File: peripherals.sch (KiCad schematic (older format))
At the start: 49 parts, among them J1 693022010811, J5 U_FL-R-SMT-1_10_, J6 U_FL-R-SMT-1_10_, J7 DM3AT-SF-PEJM5, U6 NCP163ASN330T1G, U7 EMIF06-MSD02N16

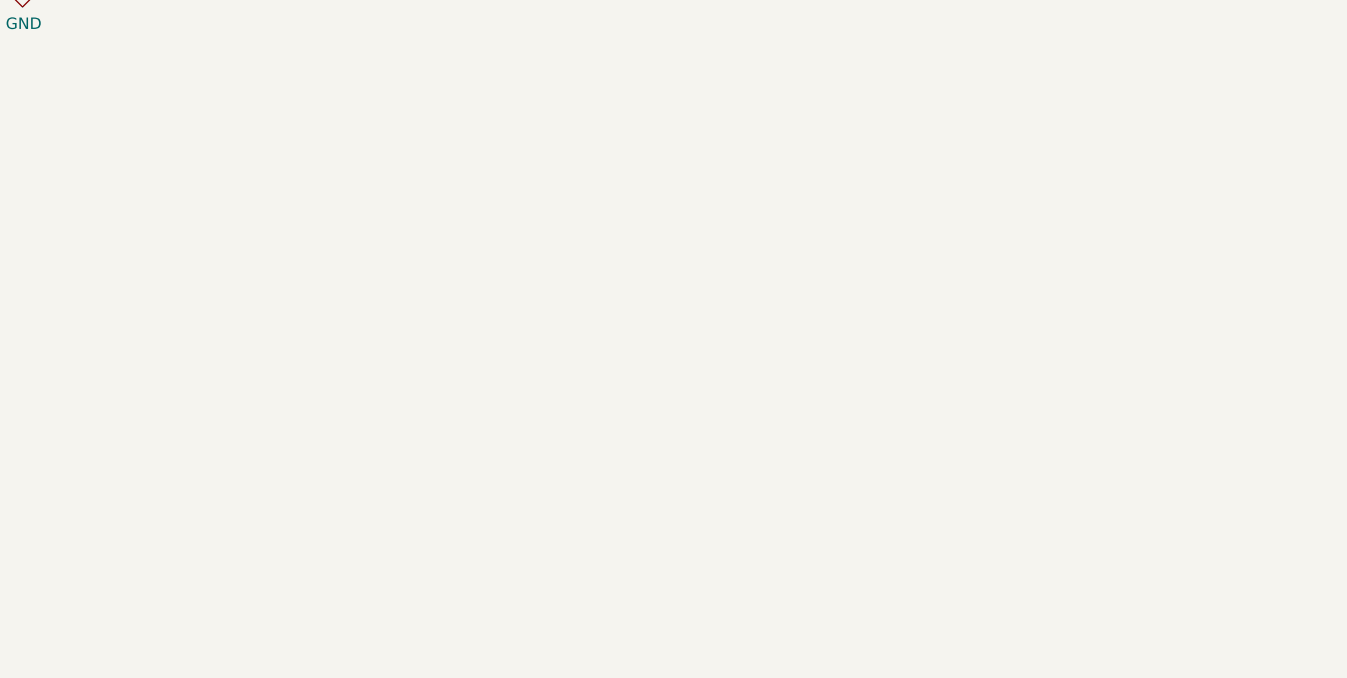
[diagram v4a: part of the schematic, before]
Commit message: Modifications after P. Szczygiel review
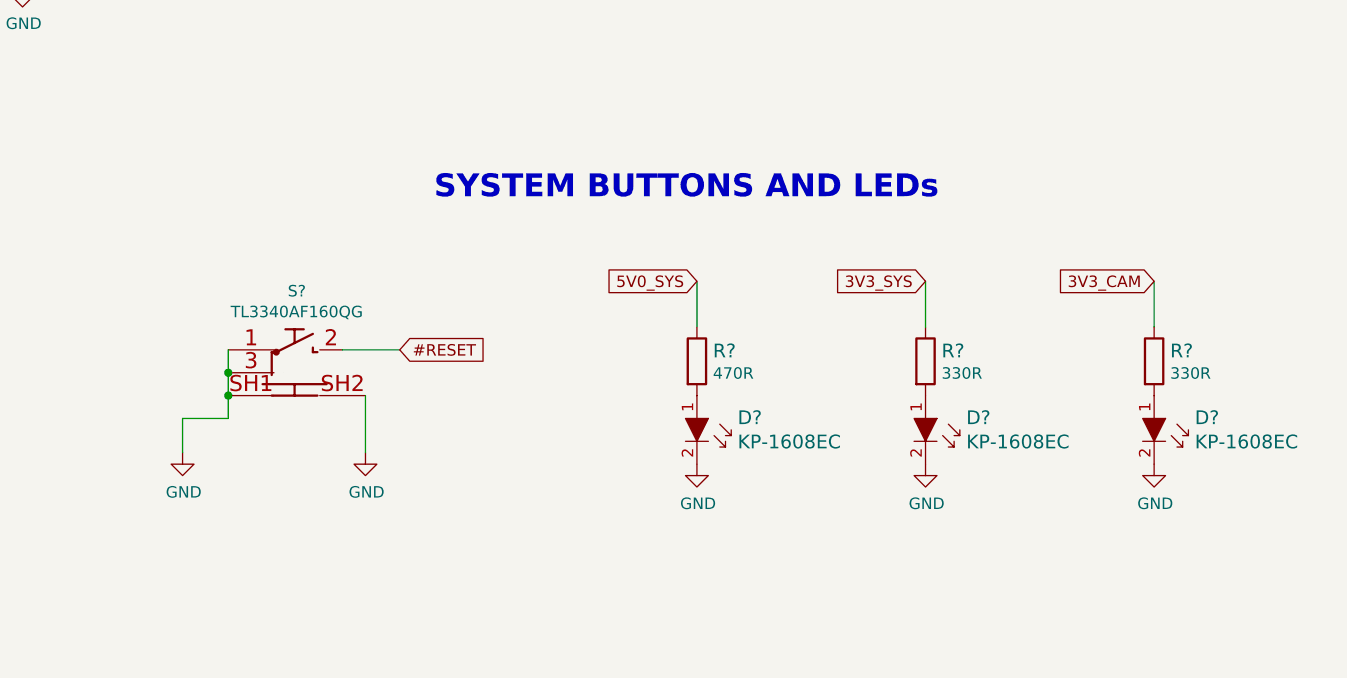
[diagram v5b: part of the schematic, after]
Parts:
- added D? (x3): KP-1608EC, antmicro-footprints:LED_0603, symbol antmicroLEDIndicationDiscrete:KP-1608EC
- added R?: R_470R_0402, antmicro-footprints:0402-res, symbol antmicroResistors0402:R_470R_0402
- added R? (x2): R_330R_0402, antmicro-footprints:0402-res, symbol antmicroResistors0402:R_330R_0402
- added S?: TL3340AF160QG, antmicro-footprints:TL3340AF160QG, symbol antmicroPushbuttonSwitches:TL3340AF160QG
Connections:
- net 5V0_SYS: now also R?.1
- net GND: now also D?.2, D?.2, D?.2, S?.1, S?.3, S?.SH1, S?.SH2
- new net: D?.1, R?.2 (x3)
- new net #RESET: S?.2
- new net 3V3_CAM: R?.1
- new net 3V3_SYS: R?.1
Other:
- note added: "SYSTEM BUTTONS AND LEDs"
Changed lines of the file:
@@
 Wire Wire Line
 	7800 8200 7800 8350
+Text Notes 11000 4700 0    100  ~ 20
+SYSTEM BUTTONS AND LEDs
+$Comp
+L power:GND #PWR?
+U 1 1 620AE84F
+P 9900 5800
+AR Path="/61D43102/620AE84F" Ref="#PWR?"  Part="1"
+AR Path="/61D49FDE/620AE84F" Ref="#PWR?"  Part="1"
+F 0 "#PWR?" H 9900 5550 50  0001 C CNN
+F 1 "GND" H 9905 5627 50  0000 C CNN
+F 2 "" H 9900 5800 50  0001 C CNN
+F 3 "" H 9900 5800 50  0001 C CNN
+	1    9900 5800
+	1    0    0    -1
+$EndComp
+Wire Wire Line
+	10100 5550 10100 5650
+Wire Wire Line
+	10100 5650 9900 5650
+Wire Wire Line
+	9900 5650 9900 5800
+Text GLabel 10850 5350 2    50   Input ~ 0
+#RESET
+$Comp
+L antmicroResistors0402:R_470R_0402 R?
+U 1 1 620AE869
+P 12150 5400
+AR Path="/61D43102/620AE869" Ref="R?"  Part="1"
+AR Path="/61D49FDE/620AE869" Ref="R?"  Part="1"
+F 0 "R?" V 12105 5470 60  0000 L CNN
+F 1 "R_470R_0402" H 12150 5250 60  0001 C CNN
+F 2 "antmicro-footprints:0402-res" H 12350 5600 60  0001 L CNN
+F 3 "" H 12150 5400 50  0001 C CNN
+F 4 "VISHAY" H 12350 5800 60  0001 L CNN "Manufacturer"
+F 5 "CRCW0402470RFKED" H 12350 5700 60  0001 L CNN "MPN"
+F 6 "470R" V 12203 5470 50  0000 L CNN "Val"
+	1    12150 5400
+	0    1    1    0
+$EndComp
+Wire Wire Line
+	12150 5250 12150 5050
+$Comp
+L antmicroLEDIndicationDiscrete:KP-1608EC D?
+U 1 1 620AE872
+P 12150 5750
+AR Path="/61D43102/620AE872" Ref="D?"  Part="1"
+AR Path="/61D49FDE/620AE872" Ref="D?"  Part="1"
+F 0 "D?" V 12047 5928 60  0000 L CNN
+F 1 "KP-1608EC" V 12153 5928 60  0000 L CNN
+F 2 "antmicro-footprints:LED_0603" H 12350 5950 60  0001 L CNN
+F 3 "https://www.farnell.com/datasheets/1854072.pdf" H 12350 6050 60  0001 L CNN
+F 4 "KP-1608EC" H 12350 6250 60  0001 L CNN "MPN"
+F 5 "KINGBRIGHT" H 12360 6370 60  0001 L CNN "Manufacturer"
+	1    12150 5750
+	0    1    1    0
+$EndComp
+$Comp
+L antmicroPushbuttonSwitches:TL3340AF160QG S?
+U 1 1 620AE879
+P 10300 5450
+AR Path="/61D43102/620AE879" Ref="S?"  Part="1"
+AR Path="/61D49FDE/620AE879" Ref="S?"  Part="1"
+F 0 "S?" H 10400 5807 50  0000 C CNN
+F 1 "TL3340AF160QG" H 10400 5716 50  0000 C CNN
+F 2 "antmicro-footprints:TL3340AF160QG" H 10300 5450 50  0001 C CNN
+F 3 "https://pl.mouser.com/datasheet/2/140/TL3340-2065742.pdf" H 10300 5450 50  0001 C CNN
+F 4 "TL3340AF160QG" H 10400 5715 50  0001 C CNN "MPN"
+	1    10300 5450
+	1    0    0    -1
+$EndComp
+Wire Wire Line
+	10100 5550 10100 5450
+Connection ~ 10100 5550
+Connection ~ 10100 5450
+Wire Wire Line
+	10100 5450 10100 5350
+$Comp
+L power:GND #PWR?
+U 1 1 620AE883
+P 10700 5800
+AR Path="/61D43102/620AE883" Ref="#PWR?"  Part="1"
+AR Path="/61D49FDE/620AE883" Ref="#PWR?"  Part="1"
+F 0 "#PWR?" H 10700 5550 50  0001 C CNN
+F 1 "GND" H 10705 5627 50  0000 C CNN
+F 2 "" H 10700 5800 50  0001 C CNN
+F 3 "" H 10700 5800 50  0001 C CNN
+	1    10700 5800
+	1    0    0    -1
+$EndComp
+Wire Wire Line
+	10700 5800 10700 5550
+Text GLabel 12150 5050 0    50   Input ~ 0
+5V0_SYS
+$Comp
+L power:GND #PWR?
+U 1 1 620AE891
+P 12150 5850
+AR Path="/61D43102/620AE891" Ref="#PWR?"  Part="1"
+AR Path="/61D49FDE/620AE891" Ref="#PWR?"  Part="1"
+F 0 "#PWR?" H 12150 5600 50  0001 C CNN
+F 1 "GND" H 12155 5677 50  0000 C CNN
+F 2 "" H 12150 5850 50  0001 C CNN
+F 3 "" H 12150 5850 50  0001 C CNN
+	1    12150 5850
+	1    0    0    -1
+$EndComp
+Wire Wire Line
+	13150 5250 13150 5050
+$Comp
+L antmicroLEDIndicationDiscrete:KP-1608EC D?
+U 1 1 620AE89A
+P 13150 5750
+AR Path="/61D43102/620AE89A" Ref="D?"  Part="1"
+AR Path="/61D49FDE/620AE89A" Ref="D?"  Part="1"
+F 0 "D?" V 13047 5928 60  0000 L CNN
+F 1 "KP-1608EC" V 13153 5928 60  0000 L CNN
+F 2 "antmicro-footprints:LED_0603" H 13350 5950 60  0001 L CNN
+F 3 "https://www.farnell.com/datasheets/1854072.pdf" H 13350 6050 60  0001 L CNN
+F 4 "KP-1608EC" H 13350 6250 60  0001 L CNN "MPN"
+F 5 "KINGBRIGHT" H 13360 6370 60  0001 L CNN "Manufacturer"
+	1    13150 5750
+	0    1    1    0
+$EndComp
+Text GLabel 13150 5050 0    50   Input ~ 0
+3V3_SYS
+$Comp
+L power:GND #PWR?
+U 1 1 620AE8A1
+P 13150 5850
+AR Path="/61D43102/620AE8A1" Ref="#PWR?"  Part="1"
+AR Path="/61D49FDE/620AE8A1" Ref="#PWR?"  Part="1"
+F 0 "#PWR?" H 13150 5600 50  0001 C CNN
+F 1 "GND" H 13155 5677 50  0000 C CNN
+F 2 "" H 13150 5850 50  0001 C CNN
+F 3 "" H 13150 5850 50  0001 C CNN
+	1    13150 5850
+	1    0    0    -1
+$EndComp
+Wire Wire Line
+	14150 5250 14150 5050
+$Comp
+L antmicroLEDIndicationDiscrete:KP-1608EC D?
+U 1 1 620AE8AA
+P 14150 5750
+AR Path="/61D43102/620AE8AA" Ref="D?"  Part="1"
+AR Path="/61D49FDE/620AE8AA" Ref="D?"  Part="1"
+F 0 "D?" V 14047 5928 60  0000 L CNN
+F 1 "KP-1608EC" V 14153 5928 60  0000 L CNN
+F 2 "antmicro-footprints:LED_0603" H 14350 5950 60  0001 L CNN
+F 3 "https://www.farnell.com/datasheets/1854072.pdf" H 14350 6050 60  0001 L CNN
+F 4 "KP-1608EC" H 14350 6250 60  0001 L CNN "MPN"
+F 5 "KINGBRIGHT" H 14360 6370 60  0001 L CNN "Manufacturer"
+	1    14150 5750
+	0    1    1    0
+$EndComp
+Text GLabel 14150 5050 0    50   Input ~ 0
+3V3_CAM
+$Comp
+L power:GND #PWR?
+U 1 1 620AE8B1
+P 14150 5850
+AR Path="/61D43102/620AE8B1" Ref="#PWR?"  Part="1"
+AR Path="/61D49FDE/620AE8B1" Ref="#PWR?"  Part="1"
+F 0 "#PWR?" H 14150 5600 50  0001 C CNN
+F 1 "GND" H 14155 5677 50  0000 C CNN
+F 2 "" H 14150 5850 50  0001 C CNN
+F 3 "" H 14150 5850 50  0001 C CNN
+	1    14150 5850
+	1    0    0    -1
+$EndComp
+$Comp
+L antmicroResistors0402:R_330R_0402 R?
+U 1 1 620AE8BA
+P 13150 5400
+AR Path="/61D43102/620AE8BA" Ref="R?"  Part="1"
+AR Path="/61D49FDE/620AE8BA" Ref="R?"  Part="1"
+F 0 "R?" V 13105 5470 60  0000 L CNN
+F 1 "R_330R_0402" H 13150 5250 60  0001 C CNN
+F 2 "antmicro-footprints:0402-res" H 13350 5600 60  0001 L CNN
+F 3 "" H 13150 5400 50  0001 C CNN
+F 4 "MULTICOMP" H 13350 5800 60  0001 L CNN "Manufacturer"
+F 5 "MCMR04X3300FTL" H 13350 5700 60  0001 L CNN "MPN"
+F 6 "330R" V 13203 5470 50  0000 L CNN "Val"
+	1    13150 5400
+	0    1    1    0
+$EndComp
+$Comp
+L antmicroResistors0402:R_330R_0402 R?
+U 1 1 620AE8C3
+P 14150 5400
+AR Path="/61D43102/620AE8C3" Ref="R?"  Part="1"
+AR Path="/61D49FDE/620AE8C3" Ref="R?"  Part="1"
+F 0 "R?" V 14105 5470 60  0000 L CNN
+F 1 "R_330R_0402" H 14150 5250 60  0001 C CNN
+F 2 "antmicro-footprints:0402-res" H 14350 5600 60  0001 L CNN
+F 3 "" H 14150 5400 50  0001 C CNN
+F 4 "MULTICOMP" H 14350 5800 60  0001 L CNN "Manufacturer"
+F 5 "MCMR04X3300FTL" H 14350 5700 60  0001 L CNN "MPN"
+F 6 "330R" V 14203 5470 50  0000 L CNN "Val"
+	1    14150 5400
+	0    1    1    0
+$EndComp
+Wire Wire Line
+	10600 5350 10850 5350
 Wire Bus Line
 	700  1450 700  2150

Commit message: Added corrections to schemas after review
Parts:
- added TP?: TestPoint, symbol Connector:TestPoint
- U7: symbol sc606-baseboard:EMIF06-MSD02N16 -> sc606-baseboard-rescue:EMIF06-MSD02N16-sc606-baseboard
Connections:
- net GND: now also U7.17 (GND), U7.18 (GND), U7.19 (GND); no longer S?.3, S?.3, S?.3
- net at U7.2 (RDAT3_GND): now also TP?.1
- net at D?.K, R?.2, S?.1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: now also S?.3 (x3)
- no-connect marks 1 -> 0
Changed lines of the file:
@@
 Connection ~ 4150 2950
 Wire Wire Line
-	3600 2950 3850 2950
-Wire Wire Line
-	3600 2850 3600 2950
-Wire Wire Line
-	3850 2850 3850 2950
-Connection ~ 3850 2950
-Wire Wire Line
-	3850 2950 4150 2950
-Wire Wire Line
 	4150 2250 4150 2650
 Wire Wire Line
 	6000 2650 6000 2950
-Connection ~ 3600 2950
 Wire Wire Line
 	3850 2050 3850 2550
@@
 	3100 9300 2950 9300
 $Comp
-L sc606-baseboard:EMIF06-MSD02N16 U7
+L sc606-baseboard-rescue:EMIF06-MSD02N16-sc606-baseboard U7
 U 1 1 61DE2B56
 P 2750 2050
+AR Path="/61DE2B56" Ref="U7"  Part="1"
+AR Path="/61D49FDE/61DE2B56" Ref="U7"  Part="1"
 F 0 "U7" H 2400 2800 50  0000 C CNN
 F 1 "EMIF06-MSD02N16" H 2700 2700 50  0000 C CNN
@@
 Wire Wire Line
 	2150 1550 2250 1550
-NoConn ~ 2250 1650
 Wire Wire Line
 	8250 1900 9000 1900
@@
 L sc606-baseboard:GND-power #PWR0123
 U 1 1 61E2FDB1
-P 7800 5700
-F 0 "#PWR0123" H 7800 5450 50  0001 C CNN
-F 1 "GND" H 7805 5527 50  0000 C CNN
-F 2 "" H 7800 5700 50  0001 C CNN
-F 3 "" H 7800 5700 50  0001 C CNN
-	1    7800 5700
-	1    0    0    -1
-$EndComp
-Wire Wire Line
-	7800 5250 7800 5400
+P 8100 5700
+F 0 "#PWR0123" H 8100 5450 50  0001 C CNN
+F 1 "GND" H 8105 5527 50  0000 C CNN
+F 2 "" H 8100 5700 50  0001 C CNN
+F 3 "" H 8100 5700 50  0001 C CNN
+	1    8100 5700
+	1    0    0    -1
+$EndComp
 Wire Wire Line
 	7800 5150 7600 5150
-Wire Wire Line
-	8100 5250 8100 5400
-Wire Wire Line
-	8100 5400 7800 5400
-Connection ~ 7800 5400
-Wire Wire Line
-	7800 5400 7800 5550
 Wire Wire Line
 	8100 5150 8100 4800
@@
 	7450 5150 7400 5150
 Wire Wire Line
-	7450 5550 7800 5550
-Connection ~ 7800 5550
-Wire Wire Line
-	7800 5550 7800 5700
+	7450 5550 8100 5550
+Connection ~ 8100 5550
+Wire Wire Line
+	8100 5550 8100 5700
 Text GLabel 6950 6550 0    50   Input ~ 0
 VOL_UP
@@
 L sc606-baseboard:GND-power #PWR0124
 U 1 1 61E6F3A3
-P 7800 7100
-F 0 "#PWR0124" H 7800 6850 50  0001 C CNN
-F 1 "GND" H 7805 6927 50  0000 C CNN
-F 2 "" H 7800 7100 50  0001 C CNN
-F 3 "" H 7800 7100 50  0001 C CNN
-	1    7800 7100
-	1    0    0    -1
-$EndComp
-Wire Wire Line
-	7800 6650 7800 6800
+P 8100 7100
+F 0 "#PWR0124" H 8100 6850 50  0001 C CNN
+F 1 "GND" H 8105 6927 50  0000 C CNN
+F 2 "" H 8100 7100 50  0001 C CNN
+F 3 "" H 8100 7100 50  0001 C CNN
+	1    8100 7100
+	1    0    0    -1
+$EndComp
 Wire Wire Line
 	7800 6550 7600 6550
-Wire Wire Line
-	8100 6650 8100 6800
-Wire Wire Line
-	8100 6800 7800 6800
-Connection ~ 7800 6800
-Wire Wire Line
-	7800 6800 7800 6950
 Wire Wire Line
 	8100 6550 8100 6200
@@
 	7450 6550 7400 6550
 Wire Wire Line
-	7450 6950 7800 6950
-Connection ~ 7800 6950
-Wire Wire Line
-	7800 6950 7800 7100
+	7450 6950 8100 6950
+Connection ~ 8100 6950
+Wire Wire Line
+	8100 6950 8100 7100
 Text GLabel 6950 7800 0    50   Input ~ 0
 VOL_DOWN
@@
 L sc606-baseboard:GND-power #PWR0125
 U 1 1 61E78409
-P 7800 8350
-F 0 "#PWR0125" H 7800 8100 50  0001 C CNN
-F 1 "GND" H 7805 8177 50  0000 C CNN
-F 2 "" H 7800 8350 50  0001 C CNN
-F 3 "" H 7800 8350 50  0001 C CNN
-	1    7800 8350
-	1    0    0    -1
-$EndComp
-Wire Wire Line
-	7800 7900 7800 8050
+P 8100 8350
+F 0 "#PWR0125" H 8100 8100 50  0001 C CNN
+F 1 "GND" H 8105 8177 50  0000 C CNN
+F 2 "" H 8100 8350 50  0001 C CNN
+F 3 "" H 8100 8350 50  0001 C CNN
+	1    8100 8350
+	1    0    0    -1
+$EndComp
 Wire Wire Line
 	7800 7800 7600 7800
-Wire Wire Line
-	8100 7900 8100 8050
-Wire Wire Line
-	8100 8050 7800 8050
-Connection ~ 7800 8050
-Wire Wire Line
-	7800 8050 7800 8200
 Wire Wire Line
 	8100 7800 8100 7450
@@
 	7450 7800 7400 7800
 Wire Wire Line
-	7450 8200 7800 8200
-Connection ~ 7800 8200
-Wire Wire Line
-	7800 8200 7800 8350
+	7450 8200 8100 8200
+Connection ~ 8100 8200
+Wire Wire Line
+	8100 8200 8100 8350
 Text Notes 11000 4700 0    100  ~ 20
 SYSTEM BUTTONS AND LEDs
@@
 Wire Wire Line
 	10600 5350 10850 5350
+Wire Wire Line
+	3600 2950 3850 2950
+Connection ~ 3850 2950
+Wire Wire Line
+	3850 2950 4150 2950
+Wire Wire Line
+	7800 5150 7800 5250
+Connection ~ 7800 5150
+Wire Wire Line
+	7800 6650 7800 6550
+Connection ~ 7800 6550
+Wire Wire Line
+	7800 7800 7800 7900
+Connection ~ 7800 7800
+Wire Wire Line
+	8100 5250 8100 5550
+Wire Wire Line
+	8100 6650 8100 6950
+Wire Wire Line
+	8100 7900 8100 8200
+$Comp
+L Connector:TestPoint TP?
+U 1 1 62632FB3
+P 2250 1650
+F 0 "TP?" V 2250 1900 50  0000 C CNN
+F 1 "TestPoint" V 2354 1722 50  0001 C CNN
+F 2 "" H 2450 1650 50  0001 C CNN
+F 3 "~" H 2450 1650 50  0001 C CNN
+	1    2250 1650
+	0    -1   -1   0
+$EndComp
 Wire Bus Line
 	700  1450 700  2150
